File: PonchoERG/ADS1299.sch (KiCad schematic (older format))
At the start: 13 parts, among them J2 I/O's Multi Propósito, U6 ADS1299

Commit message: Actualización 1.0 - Inclusión de nuevos diodos de protección TPD2E001. - Creación de librería TPD2E001 y rediseño de esquemático. - Reubicación de componentes.
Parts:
- renumbered U6 to U10
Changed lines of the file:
@@
 EESchema Schematic File Version 2
+LIBS:PonchoERG-rescue
 LIBS:74xgxx
 LIBS:74xx
@@
 LIBS:PonchoERG
 LIBS:PonchoERG-cache
-LIBS:PonchoERG-rescue
 LIBS:Power
 LIBS:VCC
@@
 $EndDescr
 $Comp
-L ADS1299 U6
+L ADS1299 U10
 U 1 1 57C2484D
 P 5500 3700
-F 0 "U6" H 4850 5350 60  0000 C CNN
+F 0 "U10" H 4850 5350 60  0000 C CNN
 F 1 "ADS1299" H 5000 1950 60  0000 C CNN
 F 2 "Housings_QFP:TQFP-64_10x10mm_Pitch0.5mm" H 5500 3700 60  0001 C CNN
@@
 $EndComp
 $Comp
-L GNDA #PWR07
+L GNDA #PWR08
 U 1 1 57C26D0E
 P 3500 4200
-F 0 "#PWR07" H 3500 3950 50  0001 C CNN
+F 0 "#PWR08" H 3500 3950 50  0001 C CNN
 F 1 "GNDA" H 3500 4050 50  0000 C CNN
 F 2 "" H 3500 4200 50  0000 C CNN
@@
 $EndComp
 $Comp
-L GNDA #PWR08
+L GNDA #PWR09
 U 1 1 57C26D36
 P 7750 3700
-F 0 "#PWR08" H 7750 3450 50  0001 C CNN
+F 0 "#PWR09" H 7750 3450 50  0001 C CNN
 F 1 "GNDA" H 7750 3550 50  0000 C CNN
 F 2 "" H 7750 3700 50  0000 C CNN
@@
 $EndComp
 $Comp
-L GNDA #PWR09
+L GNDA #PWR010
 U 1 1 57C26D7E
 P 3600 5600
-F 0 "#PWR09" H 3600 5350 50  0001 C CNN
+F 0 "#PWR010" H 3600 5350 50  0001 C CNN
 F 1 "GNDA" H 3600 5450 50  0000 C CNN
 F 2 "" H 3600 5600 50  0000 C CNN
@@
 $EndComp
 $Comp
-L GNDA #PWR010
+L GNDA #PWR011
 U 1 1 57C27023
 P 7400 2700
-F 0 "#PWR010" H 7400 2450 50  0001 C CNN
+F 0 "#PWR011" H 7400 2450 50  0001 C CNN
 F 1 "GNDA" H 7400 2550 50  0000 C CNN
 F 2 "" H 7400 2700 50  0000 C CNN
@@
 $EndComp
 $Comp
-L +5VA #PWR011
+L +5VA #PWR012
 U 1 1 57C27211
 P 3700 3700
-F 0 "#PWR011" H 3700 3550 50  0001 C CNN
+F 0 "#PWR012" H 3700 3550 50  0001 C CNN
 F 1 "+5VA" H 3700 3840 50  0000 C CNN
 F 2 "" H 3700 3700 50  0000 C CNN
@@
 $EndComp
 $Comp
-L +5VA #PWR012
+L +5VA #PWR013
 U 1 1 57C27239
 P 7100 2600
-F 0 "#PWR012" H 7100 2450 50  0001 C CNN
+F 0 "#PWR013" H 7100 2450 50  0001 C CNN
 F 1 "+5VA" H 7100 2740 50  0000 C CNN
 F 2 "" H 7100 2600 50  0000 C CNN
@@
 $EndComp
 $Comp
-L +5VA #PWR013
+L +5VA #PWR014
 U 1 1 57C27D69
 P 9000 2400
-F 0 "#PWR013" H 9000 2250 50  0001 C CNN
+F 0 "#PWR014" H 9000 2250 50  0001 C CNN
 F 1 "+5VA" H 9000 2540 50  0000 C CNN
 F 2 "" H 9000 2400 50  0000 C CNN
@@
 $EndComp
 $Comp
-L GNDA #PWR014
+L GNDA #PWR015
 U 1 1 57C27DC9
 P 9000 3100
-F 0 "#PWR014" H 9000 2850 50  0001 C CNN
+F 0 "#PWR015" H 9000 2850 50  0001 C CNN
 F 1 "GNDA" H 9000 2950 50  0000 C CNN
 F 2 "" H 9000 3100 50  0000 C CNN
@@
 NoConn ~ 4600 3800
 $Comp
-L +3.3V #PWR015
+L +3.3V #PWR016
 U 1 1 57C5E00D
 P 9900 2400
-F 0 "#PWR015" H 9900 2250 50  0001 C CNN
+F 0 "#PWR016" H 9900 2250 50  0001 C CNN
 F 1 "+3.3V" H 9900 2540 50  0000 C CNN
 F 2 "" H 9900 2400 50  0000 C CNN
@@
 $EndComp
 $Comp
-L +3.3V #PWR016
+L +3.3V #PWR017
 U 1 1 57C5ECAC
 P 6600 3800
-F 0 "#PWR016" H 6600 3650 50  0001 C CNN
+F 0 "#PWR017" H 6600 3650 50  0001 C CNN
 F 1 "+3.3V" V 6600 4050 50  0000 C CNN
 F 2 "" H 6600 3800 50  0000 C CNN
@@
 	6400 3400 6550 3400
 $Comp
-L +3.3V #PWR017
+L +3.3V #PWR018
 U 1 1 57C85F29
 P 7200 5100
-F 0 "#PWR017" H 7200 4950 50  0001 C CNN
+F 0 "#PWR018" H 7200 4950 50  0001 C CNN
 F 1 "+3.3V" H 7200 5240 50  0000 C CNN
 F 2 "" H 7200 5100 50  0000 C CNN
@@
 $EndComp
 $Comp
-L GNDD #PWR018
+L GNDD #PWR019
 U 1 1 57C8A486
 P 9900 3100
-F 0 "#PWR018" H 9900 2850 50  0001 C CNN
+F 0 "#PWR019" H 9900 2850 50  0001 C CNN
 F 1 "GNDD" H 9900 2950 50  0000 C CNN
 F 2 "" H 9900 3100 50  0000 C CNN
@@
 $EndComp
 $Comp
-L GNDD #PWR019
+L GNDD #PWR020
 U 1 1 57C8A4B4
 P 6500 5500
-F 0 "#PWR019" H 6500 5250 50  0001 C CNN
+F 0 "#PWR020" H 6500 5250 50  0001 C CNN
 F 1 "GNDD" H 6500 5350 50  0000 C CNN
 F 2 "" H 6500 5500 50  0000 C CNN
@@
 $EndComp
 $Comp
-L GNDD #PWR020
+L GNDD #PWR021
 U 1 1 57C8A4E2
 P 4500 5600
-F 0 "#PWR020" H 4500 5350 50  0001 C CNN
+F 0 "#PWR021" H 4500 5350 50  0001 C CNN
 F 1 "GNDD" H 4500 5450 50  0000 C CNN
 F 2 "" H 4500 5600 50  0000 C CNN
@@
 $EndComp
 $Comp
-L GNDD #PWR021
+L GNDD #PWR022
 U 1 1 57C8A510
 P 7200 4500
-F 0 "#PWR021" H 7200 4250 50  0001 C CNN
+F 0 "#PWR022" H 7200 4250 50  0001 C CNN
 F 1 "GNDD" V 7200 4250 50  0000 C CNN
 F 2 "" H 7200 4500 50  0000 C CNN
@@
 $EndComp
 $Comp
-L GNDD #PWR022
+L GNDD #PWR023
 U 1 1 57C8A5EC
 P 6650 3500
-F 0 "#PWR022" H 6650 3250 50  0001 C CNN
+F 0 "#PWR023" H 6650 3250 50  0001 C CNN
 F 1 "GNDD" V 6650 3250 50  0000 C CNN
 F 2 "" H 6650 3500 50  0000 C CNN

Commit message: Reubicación de ADS y componentes pasivos asociados. Sujeto a revisión.
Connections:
- net labels added: +5V
- net labels removed: +5VA
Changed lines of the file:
@@
 LIBS:ADuM2401
 LIBS:ADuM6401
-LIBS:CKCL44X7R1H
-LIBS:GNDD
 LIBS:NetTie
 LIBS:PonchoERG
 LIBS:PonchoERG-cache
-LIBS:Power
-LIBS:VCC
+LIBS:net-tie
+LIBS:TPD2E001
 EELAYER 25 0
 EELAYER END
@@
 U 1 1 57C2484D
 P 5500 3700
-F 0 "U10" H 4850 5350 60  0000 C CNN
+F 0 "U10" H 4900 5350 60  0000 C CNN
 F 1 "ADS1299" H 5000 1950 60  0000 C CNN
 F 2 "Housings_QFP:TQFP-64_10x10mm_Pitch0.5mm" H 5500 3700 60  0001 C CNN
@@
 Text HLabel 4400 2200 0    60   Input ~ 0
 IN8-
-Text HLabel 6800 1600 0    60   Input ~ 0
-IN_REF
 Text HLabel 6800 1400 0    60   Output ~ 0
 OUT_DRV_RL
@@
 $EndComp
 $Comp
-L GNDA #PWR08
-U 1 1 57C26D0E
-P 3500 4200
-F 0 "#PWR08" H 3500 3950 50  0001 C CNN
-F 1 "GNDA" H 3500 4050 50  0000 C CNN
-F 2 "" H 3500 4200 50  0000 C CNN
-F 3 "" H 3500 4200 50  0000 C CNN
-	1    3500 4200
-	-1   0    0    1
-$EndComp
-$Comp
-L GNDA #PWR09
-U 1 1 57C26D36
-P 7750 3700
-F 0 "#PWR09" H 7750 3450 50  0001 C CNN
-F 1 "GNDA" H 7750 3550 50  0000 C CNN
-F 2 "" H 7750 3700 50  0000 C CNN
-F 3 "" H 7750 3700 50  0000 C CNN
-	1    7750 3700
-	1    0    0    -1
-$EndComp
-$Comp
-L GNDA #PWR010
-U 1 1 57C26D7E
-P 3600 5600
-F 0 "#PWR010" H 3600 5350 50  0001 C CNN
-F 1 "GNDA" H 3600 5450 50  0000 C CNN
-F 2 "" H 3600 5600 50  0000 C CNN
-F 3 "" H 3600 5600 50  0000 C CNN
-	1    3600 5600
-	1    0    0    -1
-$EndComp
-$Comp
-L GNDA #PWR011
-U 1 1 57C27023
-P 7400 2700
-F 0 "#PWR011" H 7400 2450 50  0001 C CNN
-F 1 "GNDA" H 7400 2550 50  0000 C CNN
-F 2 "" H 7400 2700 50  0000 C CNN
-F 3 "" H 7400 2700 50  0000 C CNN
-	1    7400 2700
-	-1   0    0    1
-$EndComp
-$Comp
-L +5VA #PWR012
-U 1 1 57C27211
-P 3700 3700
-F 0 "#PWR012" H 3700 3550 50  0001 C CNN
-F 1 "+5VA" H 3700 3840 50  0000 C CNN
-F 2 "" H 3700 3700 50  0000 C CNN
-F 3 "" H 3700 3700 50  0000 C CNN
-	1    3700 3700
-	1    0    0    -1
-$EndComp
-$Comp
-L +5VA #PWR013
-U 1 1 57C27239
-P 7100 2600
-F 0 "#PWR013" H 7100 2450 50  0001 C CNN
-F 1 "+5VA" H 7100 2740 50  0000 C CNN
-F 2 "" H 7100 2600 50  0000 C CNN
-F 3 "" H 7100 2600 50  0000 C CNN
-	1    7100 2600
-	1    0    0    -1
-$EndComp
-$Comp
 L C C26
 U 1 1 57C27C51
@@
 F 3 "" H 10100 2750 50  0000 C CNN
 	1    10100 2750
-	1    0    0    -1
-$EndComp
-$Comp
-L +5VA #PWR014
-U 1 1 57C27D69
-P 9000 2400
-F 0 "#PWR014" H 9000 2250 50  0001 C CNN
-F 1 "+5VA" H 9000 2540 50  0000 C CNN
-F 2 "" H 9000 2400 50  0000 C CNN
-F 3 "" H 9000 2400 50  0000 C CNN
-	1    9000 2400
-	1    0    0    -1
-$EndComp
-$Comp
-L GNDA #PWR015
-U 1 1 57C27DC9
-P 9000 3100
-F 0 "#PWR015" H 9000 2850 50  0001 C CNN
-F 1 "GNDA" H 9000 2950 50  0000 C CNN
-F 2 "" H 9000 3100 50  0000 C CNN
-F 3 "" H 9000 3100 50  0000 C CNN
-	1    9000 3100
 	1    0    0    -1
 $EndComp
@@
 NoConn ~ 4600 3900
 NoConn ~ 4600 3800
-$Comp
-L +3.3V #PWR016
-U 1 1 57C5E00D
-P 9900 2400
-F 0 "#PWR016" H 9900 2250 50  0001 C CNN
-F 1 "+3.3V" H 9900 2540 50  0000 C CNN
-F 2 "" H 9900 2400 50  0000 C CNN
-F 3 "" H 9900 2400 50  0000 C CNN
-	1    9900 2400
-	1    0    0    -1
-$EndComp
-$Comp
-L +3.3V #PWR017
-U 1 1 57C5ECAC
-P 6600 3800
-F 0 "#PWR017" H 6600 3650 50  0001 C CNN
-F 1 "+3.3V" V 6600 4050 50  0000 C CNN
-F 2 "" H 6600 3800 50  0000 C CNN
-F 3 "" H 6600 3800 50  0000 C CNN
-	1    6600 3800
-	0    1    1    0
-$EndComp
 Wire Wire Line
 	4400 2200 4600 2200
@@
 Wire Wire Line
 	6400 3400 6550 3400
-$Comp
-L +3.3V #PWR018
-U 1 1 57C85F29
-P 7200 5100
-F 0 "#PWR018" H 7200 4950 50  0001 C CNN
-F 1 "+3.3V" H 7200 5240 50  0000 C CNN
-F 2 "" H 7200 5100 50  0000 C CNN
-F 3 "" H 7200 5100 50  0000 C CNN
-	1    7200 5100
-	1    0    0    -1
-$EndComp
-$Comp
-L GNDD #PWR019
-U 1 1 57C8A486
-P 9900 3100
-F 0 "#PWR019" H 9900 2850 50  0001 C CNN
-F 1 "GNDD" H 9900 2950 50  0000 C CNN
-F 2 "" H 9900 3100 50  0000 C CNN
-F 3 "" H 9900 3100 50  0000 C CNN
-	1    9900 3100
-	1    0    0    -1
-$EndComp
-$Comp
-L GNDD #PWR020
-U 1 1 57C8A4B4
-P 6500 5500
-F 0 "#PWR020" H 6500 5250 50  0001 C CNN
-F 1 "GNDD" H 6500 5350 50  0000 C CNN
-F 2 "" H 6500 5500 50  0000 C CNN
-F 3 "" H 6500 5500 50  0000 C CNN
-	1    6500 5500
-	1    0    0    -1
-$EndComp
-$Comp
-L GNDD #PWR021
-U 1 1 57C8A4E2
-P 4500 5600
-F 0 "#PWR021" H 4500 5350 50  0001 C CNN
-F 1 "GNDD" H 4500 5450 50  0000 C CNN
-F 2 "" H 4500 5600 50  0000 C CNN
-F 3 "" H 4500 5600 50  0000 C CNN
-	1    4500 5600
-	1    0    0    -1
-$EndComp
-$Comp
-L GNDD #PWR022
-U 1 1 57C8A510
-P 7200 4500
-F 0 "#PWR022" H 7200 4250 50  0001 C CNN
-F 1 "GNDD" V 7200 4250 50  0000 C CNN
-F 2 "" H 7200 4500 50  0000 C CNN
-F 3 "" H 7200 4500 50  0000 C CNN
-	1    7200 4500
-	0    -1   -1   0
-$EndComp
-$Comp
-L GNDD #PWR023
-U 1 1 57C8A5EC
-P 6650 3500
-F 0 "#PWR023" H 6650 3250 50  0001 C CNN
-F 1 "GNDD" V 6650 3250 50  0000 C CNN
-F 2 "" H 6650 3500 50  0000 C CNN
-F 3 "" H 6650 3500 50  0000 C CNN
-	1    6650 3500
-	0    -1   -1   0
-$EndComp
+Text HLabel 6800 1600 0    60   Input ~ 0
+IN_REF
+Text GLabel 9000 2400 1    60   Input ~ 0
++3.3V
+Text GLabel 7100 2600 1    60   Input ~ 0
++3.3V
+Text GLabel 3700 3700 1    60   Input ~ 0
++3.3V
+Text GLabel 6600 3800 2    60   Input ~ 0
++3.3V
+Text GLabel 7200 5100 2    60   Input ~ 0
++3.3V
+Text GLabel 9000 3100 3    60   Output ~ 0
+GNDD
+Text GLabel 6500 5500 3    60   Output ~ 0
+GNDD
+Text GLabel 4500 5600 3    60   Output ~ 0
+GNDD
+Text GLabel 7200 4500 2    60   Output ~ 0
+GNDD
+Text GLabel 6650 3500 2    60   Output ~ 0
+GNDD
+Text GLabel 9900 3100 3    60   Output ~ 0
+GNDA
+Text GLabel 3500 4200 1    60   Output ~ 0
+GNDA
+Text GLabel 7400 2700 1    60   Output ~ 0
+GNDA
+Text GLabel 3600 5600 3    60   Output ~ 0
+GNDA
+Text GLabel 7750 3700 3    60   Output ~ 0
+GNDA
+Text GLabel 9900 2400 1    60   Input ~ 0
++5V
 $EndSCHEMATC

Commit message: Subida n.0
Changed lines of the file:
@@
 	3900 5100 4600 5100
 Wire Wire Line
-	6400 3800 6600 3800
+	6400 3800 7050 3800
 Wire Wire Line
 	6400 3600 6550 3600
@@
 Text GLabel 3700 3700 1    60   Input ~ 0
 +3.3V
-Text GLabel 6600 3800 2    60   Input ~ 0
+Text GLabel 7050 3800 2    60   Input ~ 0
 +3.3V
 Text GLabel 7200 5100 2    60   Input ~ 0
@@
 Text GLabel 9900 2400 1    60   Input ~ 0
 +5V
+Text Label 6650 3800 0    60   ~ 0
+¡33333
 $EndSCHEMATC

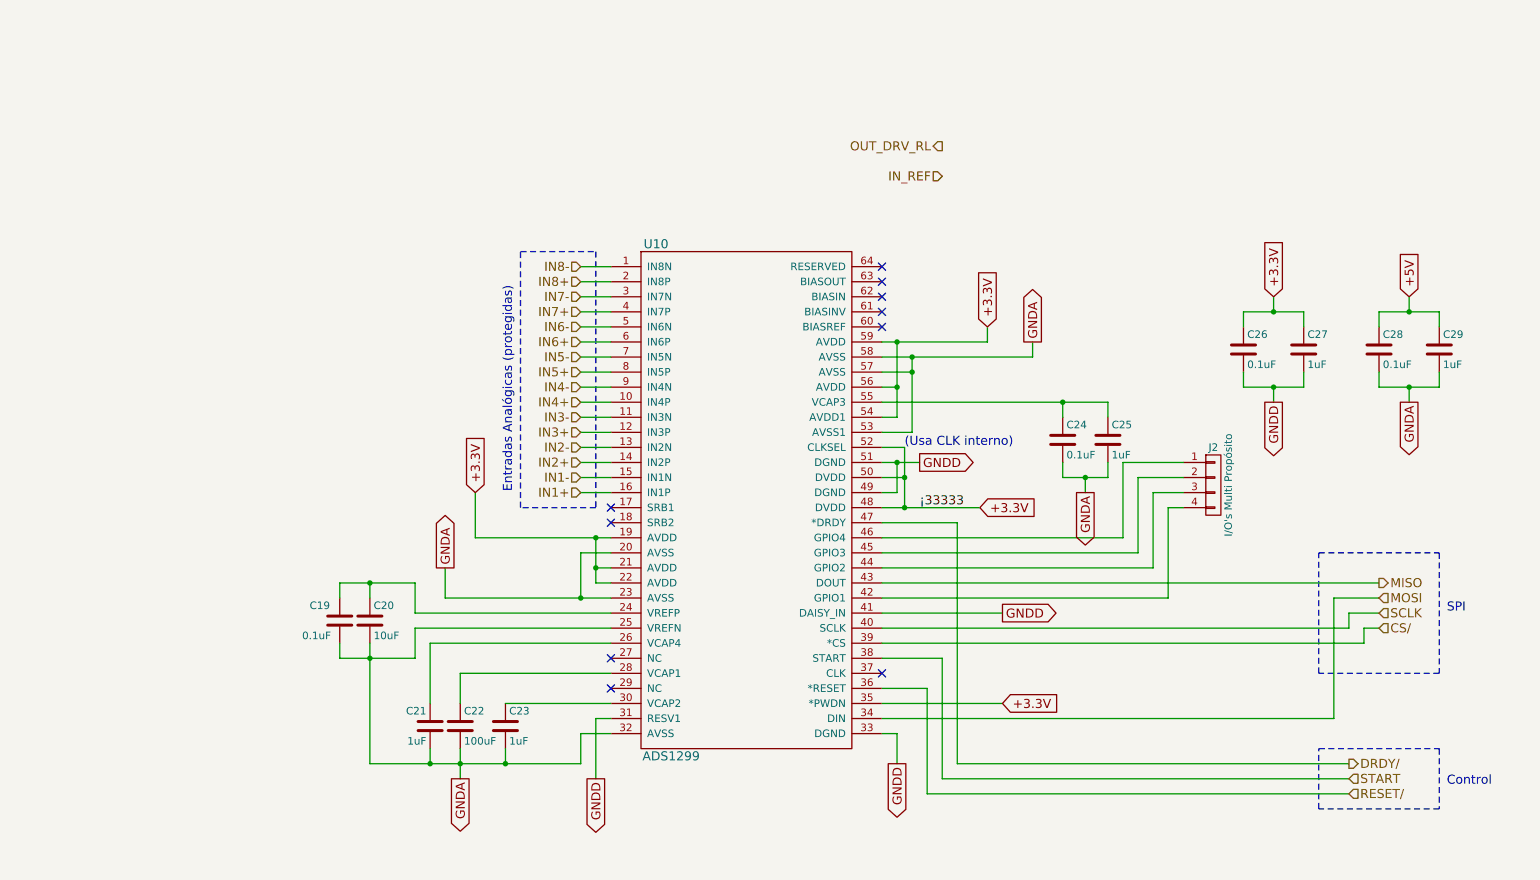
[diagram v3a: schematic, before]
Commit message: Última actualización del proyecto. Creación de librería única "PonchoERG.lib" con todos los componentes. Se agregó el conector estilo CIAA para conectar SPI y alimentaciones. Se agregó carpeta con archivos para creación de lista de materiales "PonchoERG.xml" provisoria. Se modificaron todos los pines de alimentación que estaban como etiquetas con los correspondientes. Quedaría solucionar los problemas del ERC respecto a los errores de pines con el famoso PWR_FLAG.
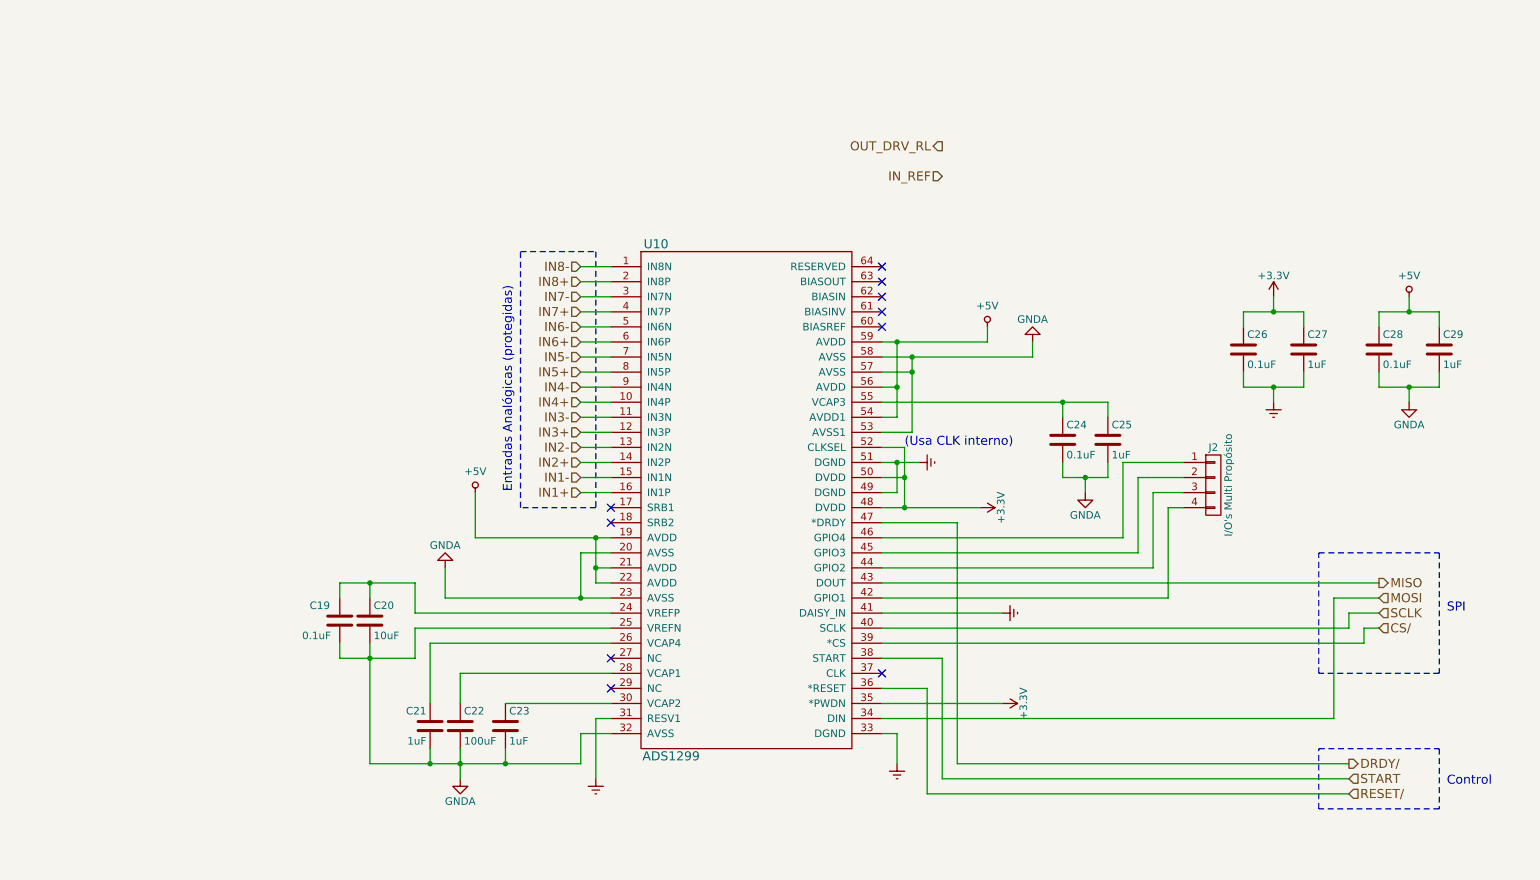
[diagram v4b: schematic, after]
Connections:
- net +5V: now also U10.19 (AVDD), U10.21 (AVDD), U10.22 (AVDD), U10.54 (AVDD1), U10.56 (AVDD), U10.59 (AVDD)
- net +3.3V renamed +3V3
- net +3V3: no longer U10.19 (AVDD), U10.21 (AVDD), U10.22 (AVDD), U10.54 (AVDD1), U10.56 (AVDD), U10.59 (AVDD)
- net GNDD renamed Earth

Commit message: Inclusión en esquemáticos de los nuevos bloques de circuitos para la utilización de las líneas del BIAS. Actualización de librería de proyecto. Objetivo de este comit: revisar actualización e inclusión de BIAS.
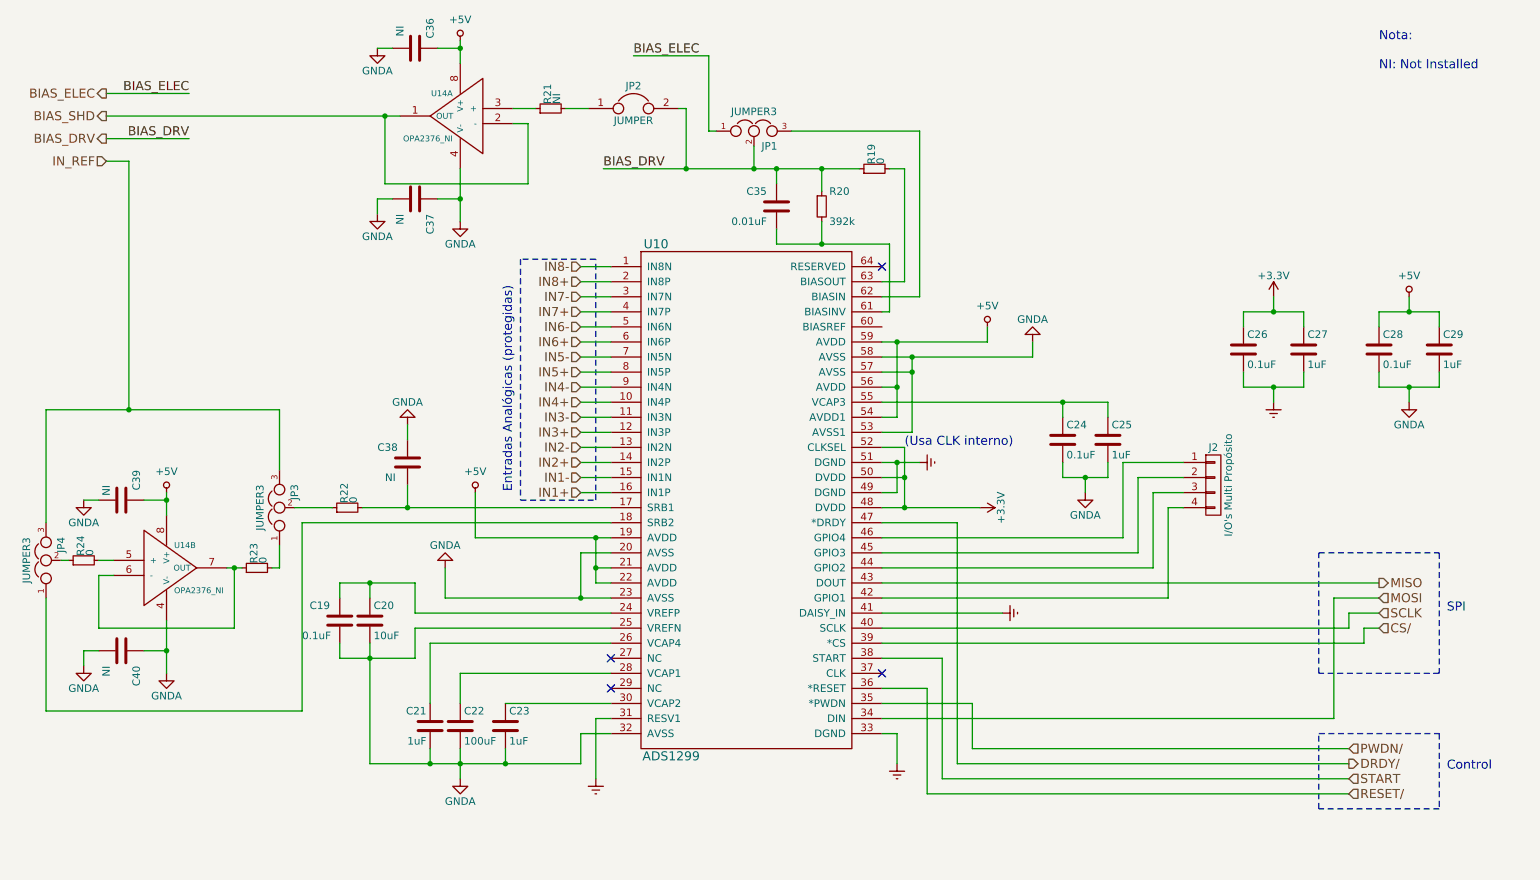
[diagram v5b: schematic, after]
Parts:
- added C35: 0.01uF, symbol C
- added C36, C37, C38, C39, C40: NI, symbol C
- added JP1, JP3, JP4: JUMPER3, symbol JUMPER3
- added JP2: JUMPER, symbol JUMPER
- added R19, R22, R23, R24: 0, symbol R_Small
- added R20: 392k, symbol R_Small
- added R21: NI, symbol R_Small
- added U14: OPA2376_NI, symbol OPA2376
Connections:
- net +3V3: no longer U10.35 (*PWDN)
- net +5V: now also C36.1, C39.1, U14.8 (V+), U14.8 (V+)
- net GNDA: now also C36.2, C37.1, C37.2, C38.1, C39.2, C40.1, C40.2, U14.4 (V-), U14.4 (V-)
- net IN_REF: now also JP3.3, JP4.3
- net at U10.17 (SRB1): now also C38.2, R22.2
- net at U10.18 (SRB2): now also JP4.1
- net at U10.61 (BIASINV): now also C35.2, R20.2
- net at U10.62 (BIASIN): now also JP1.3
- net at U10.63 (BIASOUT): now also R19.2
- new net: JP2.1, R21.2
- new net: R21.1, U14.3 (+)
- new net: R24.2, U14.5 (+)
- new net: R23.1, U14.6 (-), U14.7 (OUT)
- new net: JP3.1, R23.2
- new net: JP3.2, R22.1
- new net: JP4.2, R24.1
- new net BIAS_DRV: C35.1, JP1.2, JP2.2, R19.1, R20.1
- new net BIAS_ELEC: JP1.1
- new net BIAS_SHD: U14.1 (OUT), U14.2 (-)
- new net PWDN/: U10.35 (*PWDN)
- no-connect marks 10 -> 4
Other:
- note added: "Nota:\n\nNI: Not Installed"
